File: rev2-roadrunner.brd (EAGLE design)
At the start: 49.5 x 34.3 mm, 22 parts, among them J1 USB_MINI-B_SMT, Y1 16MHz

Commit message: Finalized Board and Schematic design
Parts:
- added C4: 0.1uF, SparkFun-Capacitors:1206
- added C5: 1.0uF, SparkFun-Capacitors:1206
- added D4: WS2812B, SparkFun-LED:WS2812B
- added F1: 6V/0.5A, SparkFun-Fuses:1206
- D7: value GREEN -> Yellow
- J2: device SparkFun-Connectors:1X03 -> SparkFun-Connectors:1X07
- J3: device SparkFun-Connectors:1X14 -> SparkFun-Connectors:1X10
- J4: device SparkFun-Connectors:1X04 -> SparkFun-Connectors:1X06
- moved J4 43.9 mm to (3.30, 2.16), turned to 0 degrees
- moved J3 29.5 mm to (47.0, 2.54), turned to 90 degrees
- moved R7 25.0 mm to (36.9, 9.43), turned to 180 degrees
- moved D1 23.4 mm to (27.1, 30.7)
- moved R3 21.0 mm to (24.4, 30.8), turned to 270 degrees
- moved D7 19.2 mm to (36.9, 12.7)
- moved S1 18.3 mm to (37.5, 4.03), turned to 0 degrees
- moved C1 13.7 mm to (14.0, 25.9), turned to 180 degrees
- moved J2 11.9 mm to (47.0, 31.8), turned to 180 degrees
- moved D3 10.7 mm to (5.59, 32.0), turned to 180 degrees
- moved C2 5.18 mm to (12.7, 30.5), turned to 90 degrees
- moved R8 4.05 mm to (13.9, 9.27), turned to 0 degrees
- moved ICSP 2.54 mm to (6.00, 9.04)
- moved D2 2.51 mm to (14.2, 12.3), turned to 180 degrees
- moved R4 2.36 mm to (13.9, 22.1)
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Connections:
- net USBD1_N renamed USB_D1_N
- net USBD1_P renamed USB_D1_P
- net USBD_N renamed USB_D_N
- net USBD_P renamed USB_D_P
- new net N$4: D3.A, F1.2
- new net USB_VCC: F1.1, J1.VBUS
- net 5V: now also C2.1, C4.1, C5.1, D2.A, D4.1, D7.A, J2.7, R3.2; no longer C2.2, J1.VBUS, J3.14, R7.2
- net AREF: now also J2.5; no longer J3.12
- net GND: now also C2.2, C4.2, C5.2, D4.3, J2.6; no longer C2.1, D2.C, D3.A, D7.C, J3.13
- net N$2: now also D7.C, R7.1; no longer D2.A, R2.1
- net N$3: now also D2.C, R2.2; no longer D7.A, R7.1
- net PB4: now also J3.4; no longer J3.1
- net PB5: now also J3.5; no longer J3.2
- net PB6: now also J3.6; no longer J3.3
- net PB7: now also J4.6
- net PC6: now also J3.7; no longer J3.4
- net PC7: now also J3.8; no longer J3.5
- net PD4: now also J3.1; no longer J2.1
- net PD6: now also J3.2; no longer J2.2
- net PD7: now also J3.3; no longer J2.3
- net PE6: now also J4.5
- net PF0: now also J2.4; no longer J3.11
- net PF1: now also J2.3; no longer J3.10
- net PF4: now also J2.2; no longer J3.9
- net PF5: now also J2.1; no longer J3.8
- net PF6: now also J3.10; no longer J3.7
- net PF7: now also D4.4, J3.9; no longer J3.6
- net RX_LED: now also R2.1; no longer R2.2
- net TX_LED: now also R7.2; no longer R3.2
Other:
- board text added: "IEEE Carleton PCB Workshop Fall 2017"
- board text added: "PB7"
- board text added: "PE6"
- board text added: "RoadRunner"

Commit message: Before Autorouter
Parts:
- moved R1 0.25 mm to (13.9, 18.3)
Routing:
- net 5V: track 0.00 -> 24.9 mm
- net XTAL_N: track 0.00 -> 9.36 mm
- net XTAL_P: track 0.00 -> 9.27 mm
- net USB_VCC: track 0.00 -> 8.90 mm
- net USB_D1_N: track 0.00 -> 5.25 mm
- net USB_D1_P: track 0.00 -> 5.22 mm
- net USB_D_N: track 0.00 -> 4.67 mm
- net USB_D_P: track 0.00 -> 4.64 mm
- net N$4: track 0.00 -> 3.66 mm
- net N$1: track 0.00 -> 2.73 mm
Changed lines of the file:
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@@
 <?xml version="1.0" encoding="utf-8"?>
 <!DOCTYPE eagle SYSTEM "eagle.dtd">
-<eagle version="8.3.0">
+<eagle version="8.2.2">
 <drawing>
 <settings>
 <setting alwaysvectorfont="no"/>
-<setting keepoldvectorfont="yes"/>
 <setting verticaltext="up"/>
 </settings>
-<grid distance="0.05" unitdist="inch" unit="mil" style="lines" multiple="1" display="yes" altdistance="0.005" altunitdist="inch" altunit="mil"/>
+<grid distance="50" unitdist="mil" unit="mil" style="lines" multiple="1" display="yes" altdistance="0.005" altunitdist="inch" altunit="mil"/>
 <layers>
 <layer number="1" name="Top" color="4" fill="1" visible="yes" active="yes"/>
@@
 <attribute name="PROD_ID" value="CAP-10057" x="12.667284375" y="30.4521625" size="1.778" layer="27" rot="R90" display="off"/>
 </element>
-<element name="R1" library="SparkFun-Resistors" package="1206" value=" 22" x="13.9421625" y="18.574715625" smashed="yes">
-<attribute name="NAME" x="14.0691625" y="17.177715625" size="0.6096" layer="25" font="vector" ratio="20" align="bottom-center"/>
-<attribute name="PROD_ID" value=" " x="13.9421625" y="18.574715625" size="1.778" layer="27" display="off"/>
+<element name="R1" library="SparkFun-Resistors" package="1206" value=" 22" x="13.9421625" y="18.320715625" smashed="yes">
+<attribute name="NAME" x="14.0691625" y="16.923715625" size="0.6096" layer="25" font="vector" ratio="20" align="bottom-center"/>
+<attribute name="PROD_ID" value=" " x="13.9421625" y="18.320715625" size="1.778" layer="27" display="off"/>
 </element>
 <element name="R4" library="SparkFun-Resistors" package="1206" value=" 22" x="13.9421625" y="22.130715625" smashed="yes">
@@
 <contactref element="Y1" pad="1"/>
 <contactref element="C3" pad="2"/>
-<wire x1="27.0201625" y1="9.303715625" x2="25.7531625" y2="12.393715625" width="0" layer="19" extent="1-1"/>
-<wire x1="27.7851625" y1="3.969715625" x2="27.0201625" y2="9.303715625" width="0" layer="19" extent="1-1"/>
+<wire x1="25.7531625" y1="12.393715625" x2="25.7531625" y2="10.570715625" width="0.254" layer="1"/>
+<wire x1="25.7531625" y1="10.570715625" x2="27.0201625" y2="9.303715625" width="0.254" layer="1"/>
+<wire x1="27.0201625" y1="9.303715625" x2="27.0201625" y2="4.734715625" width="0.254" layer="1"/>
+<wire x1="27.0201625" y1="4.734715625" x2="27.7851625" y2="3.969715625" width="0.254" layer="1"/>
 </signal>
 <signal name="XTAL_N">
@@
 <contactref element="Y1" pad="2"/>
 <contactref element="C6" pad="2"/>
-<wire x1="23.7241625" y1="9.303715625" x2="24.9531625" y2="12.393715625" width="0" layer="19" extent="1-1"/>
-<wire x1="22.7051625" y1="3.969715625" x2="23.7241625" y2="9.303715625" width="0" layer="19" extent="1-1"/>
+<wire x1="24.9531625" y1="12.393715625" x2="24.9531625" y2="10.532715625" width="0.254" layer="1"/>
+<wire x1="24.9531625" y1="10.532715625" x2="23.7241625" y2="9.303715625" width="0.254" layer="1"/>
+<wire x1="23.7241625" y1="9.303715625" x2="23.7241625" y2="4.988715625" width="0.254" layer="1"/>
+<wire x1="23.7241625" y1="4.988715625" x2="22.7051625" y2="3.969715625" width="0.254" layer="1"/>
 </signal>
 <signal name="MISO">
@@
 <contactref element="J2" pad="7"/>
 <contactref element="D4" pad="1"/>
+<wire x1="6.738" y1="32.004" x2="7.366" y2="32.004" width="0.508" layer="1"/>
+<wire x1="7.366" y1="32.004" x2="10.16" y2="29.21" width="0.508" layer="1"/>
+<wire x1="10.16" y1="29.21" x2="12.509446875" y2="29.21" width="0.508" layer="1"/>
+<wire x1="12.509446875" y1="29.21" x2="12.667284375" y2="29.0521625" width="0.508" layer="1"/>
+<wire x1="12.667284375" y1="29.0521625" x2="15.8471625" y2="29.0521625" width="0.508" layer="1"/>
+<wire x1="15.8471625" y1="29.0521625" x2="15.875" y2="29.08" width="0.508" layer="1"/>
+<wire x1="15.875" y1="29.08" x2="19.685" y2="29.08" width="0.508" layer="1"/>
+<wire x1="19.685" y1="29.08" x2="19.685" y2="26.061878125" width="0.508" layer="1"/>
+<wire x1="19.685" y1="26.061878125" x2="21.7531625" y2="23.993715625" width="0.508" layer="1"/>
+<wire x1="19.685" y1="29.08" x2="24.029871875" y2="29.08" width="0.508" layer="1"/>
+<wire x1="24.029871875" y1="29.08" x2="24.351284375" y2="29.4014125" width="0.508" layer="1"/>
 <wire x1="24.351284375" y1="29.4014125" x2="31.75" y2="31.75" width="0" layer="19" extent="1-1"/>
-<wire x1="19.685" y1="29.08" x2="24.351284375" y2="29.4014125" width="0" layer="19" extent="1-1"/>
-<wire x1="15.875" y1="29.08" x2="19.685" y2="29.08" width="0" layer="19" extent="1-1"/>
-<wire x1="12.667284375" y1="29.0521625" x2="15.875" y2="29.08" width="0" layer="19" extent="1-1"/>
-<wire x1="21.7531625" y1="23.993715625" x2="19.685" y2="29.08" width="0" layer="19" extent="1-1"/>
 <wire x1="19.9531625" y1="21.393715625" x2="21.7531625" y2="23.993715625" width="0" layer="19" extent="1-1"/>
 <wire x1="19.9531625" y1="17.393715625" x2="19.9531625" y2="21.393715625" width="0" layer="19" extent="1-1"/>
 <wire x1="23.3531625" y1="12.393715625" x2="19.9531625" y2="17.393715625" width="0" layer="19" extent="1-1"/>
-<wire x1="6.738" y1="32.004" x2="12.667284375" y2="29.0521625" width="0" layer="19" extent="1-1"/>
 <wire x1="15.691284375" y1="12.2911625" x2="19.9531625" y2="17.393715625" width="0" layer="19" extent="1-1"/>
 <wire x1="15.3421625" y1="9.271965625" x2="15.691284375" y2="12.2911625" width="0" layer="19" extent="1-1"/>
 <wire x1="29.7531625" y1="23.993715625" x2="24.351284375" y2="29.4014125" width="0" layer="19" extent="1-1"/>
-<wire x1="31.5531625" y1="14.993715625" x2="23.3531625" y2="12.393715625" width="0" layer="19" extent="1-1"/>
+<wire x1="35.484" y1="20.41" x2="29.7531625" y2="23.993715625" width="0" layer="19" extent="1-1"/>
+<wire x1="31.5531625" y1="14.993715625" x2="35.484" y2="20.41" width="0" layer="19" extent="1-1"/>
 <wire x1="35.424284375" y1="12.6721625" x2="31.5531625" y2="14.993715625" width="0" layer="19" extent="1-1"/>
-<wire x1="35.484" y1="20.41" x2="29.7531625" y2="23.993715625" width="0" layer="19" extent="1-1"/>
 <wire x1="4.731715625" y1="6.5048375" x2="15.3421625" y2="9.271965625" width="0" layer="19" extent="1-1"/>
 </signal>
@@
 <contactref element="R3" pad="1"/>
 <contactref element="D1" pad="A"/>
-<wire x1="24.351284375" y1="32.2014125" x2="27.0788375" y2="32.201284375" width="0" layer="19" extent="1-1"/>
+<wire x1="24.351284375" y1="32.2014125" x2="27.078709375" y2="32.2014125" width="0.508" layer="1"/>
+<wire x1="27.078709375" y1="32.2014125" x2="27.0788375" y2="32.201284375" width="0.508" layer="1"/>
 </signal>
 <signal name="RX_LED">
@@
 <contactref element="J1" pad="D-"/>
 <contactref element="R4" pad="1"/>
-<wire x1="8.514315625" y1="20.589015625" x2="12.5421625" y2="22.130715625" width="0" layer="19" extent="1-1"/>
+<wire x1="8.514315625" y1="20.589015625" x2="11.0004625" y2="20.589015625" width="0.508" layer="1"/>
+<wire x1="11.0004625" y1="20.589015625" x2="12.5421625" y2="22.130715625" width="0.508" layer="1"/>
 </signal>
 <signal name="USB_VCC" class="3">
 <contactref element="J1" pad="VBUS"/>
 <contactref element="F1" pad="1"/>
-<wire x1="8.514315625" y1="21.389015625" x2="7.496" y2="28.448" width="0" layer="19" extent="1-1"/>
+<wire x1="7.496" y1="28.448" x2="7.496" y2="28.2039125" width="0.508" layer="1"/>
+<wire x1="7.496" y1="28.2039125" x2="10.221515625" y2="25.478396875" width="0.508" layer="1"/>
+<wire x1="10.221515625" y1="23.096215625" x2="8.514315625" y2="21.389015625" width="0.508" layer="1"/>
+<wire x1="10.221515625" y1="25.478396875" x2="10.221515625" y2="23.096215625" width="0.508" layer="1"/>
 </signal>
 <signal name="USB_D_P">
 <contactref element="J1" pad="D+"/>
 <contactref element="R1" pad="1"/>
-<wire x1="8.514315625" y1="19.789015625" x2="12.5421625" y2="18.574715625" width="0" layer="19" extent="1-1"/>
+<wire x1="8.514315625" y1="19.789015625" x2="11.0738625" y2="19.789015625" width="0.508" layer="1"/>
+<wire x1="11.0738625" y1="19.789015625" x2="12.5421625" y2="18.320715625" width="0.508" layer="1"/>
 </signal>
 <signal name="USB_D1_P">
 <contactref element="R1" pad="2"/>
 <contactref element="U$1" pad="4"/>
-<wire x1="15.3421625" y1="18.574715625" x2="19.9531625" y2="19.793715625" width="0" layer="19" extent="1-1"/>
+<wire x1="19.9531625" y1="19.793715625" x2="16.8151625" y2="19.793715625" width="0.508" layer="1"/>
+<wire x1="16.8151625" y1="19.793715625" x2="15.3421625" y2="18.320715625" width="0.508" layer="1"/>
 </signal>
 <signal name="USB_D1_N">
 <contactref element="R4" pad="2"/>
 <contactref element="U$1" pad="3"/>
-<wire x1="15.3421625" y1="22.130715625" x2="19.9531625" y2="20.593715625" width="0" layer="19" extent="1-1"/>
+<wire x1="19.9531625" y1="20.593715625" x2="16.8791625" y2="20.593715625" width="0.508" layer="1"/>
+<wire x1="16.8791625" y1="20.593715625" x2="15.3421625" y2="22.130715625" width="0.508" layer="1"/>
 </signal>
 <signal name="N$4">
 <contactref element="F1" pad="2"/>
 <contactref element="D3" pad="A"/>
-<wire x1="4.696" y1="28.448" x2="4.438" y2="32.004" width="0" layer="19" extent="1-1"/>
+<wire x1="4.438" y1="32.004" x2="4.438" y2="28.706" width="0.508" layer="1"/>
+<wire x1="4.438" y1="28.706" x2="4.696" y2="28.448" width="0.508" layer="1"/>
 </signal>
 <signal name="N$2">
@@
 </note>
 <note version="8.2" severity="warning">
-Since Version 8.2, EAGLE supports online libraries. The ids
+Since Version 8.2, Eagle supports online libraries. The ids
 of those online libraries will not be understood (or retained)
 with this version.

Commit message: Fixed Routes after Autorouter
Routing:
- net 5V: track 24.9 -> 102.3 mm
- net PD1: track 0.00 -> 48.7 mm, vias 0 -> 1
- net RST: track 0.00 -> 45.0 mm, vias 0 -> 1
- net PE6: track 0.00 -> 40.6 mm, vias 0 -> 1
- net PD0: track 0.00 -> 36.3 mm, vias 0 -> 2
- net PD7: track 0.00 -> 34.8 mm
- net TX: track 0.00 -> 33.9 mm
- net PB4: track 0.00 -> 31.5 mm, vias 0 -> 1
- net PF4: track 0.00 -> 29.0 mm, vias 0 -> 1
- net PD6: track 0.00 -> 28.8 mm, vias 0 -> 1
- net RX: track 0.00 -> 28.3 mm, vias 0 -> 1
- net PD4: track 0.00 -> 26.0 mm, vias 0 -> 1
- net PF5: track 0.00 -> 24.8 mm, vias 0 -> 2
- net PF0: track 0.00 -> 24.2 mm, vias 0 -> 1
- net PF1: track 0.00 -> 23.7 mm, vias 0 -> 1
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- added copper zone on layer 1, net GND
- added copper zone on layer 16, net GND
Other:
- board text added: "VCC"

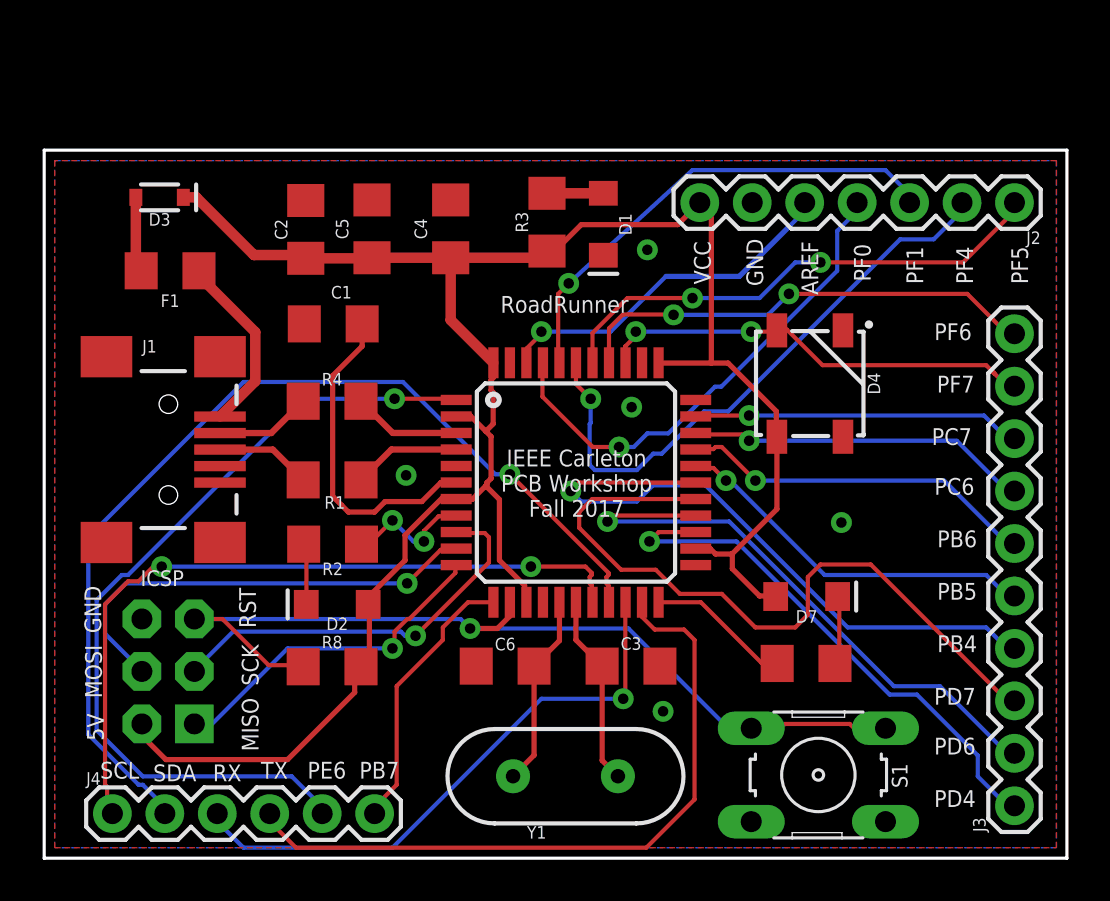
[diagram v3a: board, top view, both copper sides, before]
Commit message: Added attributes for crystal
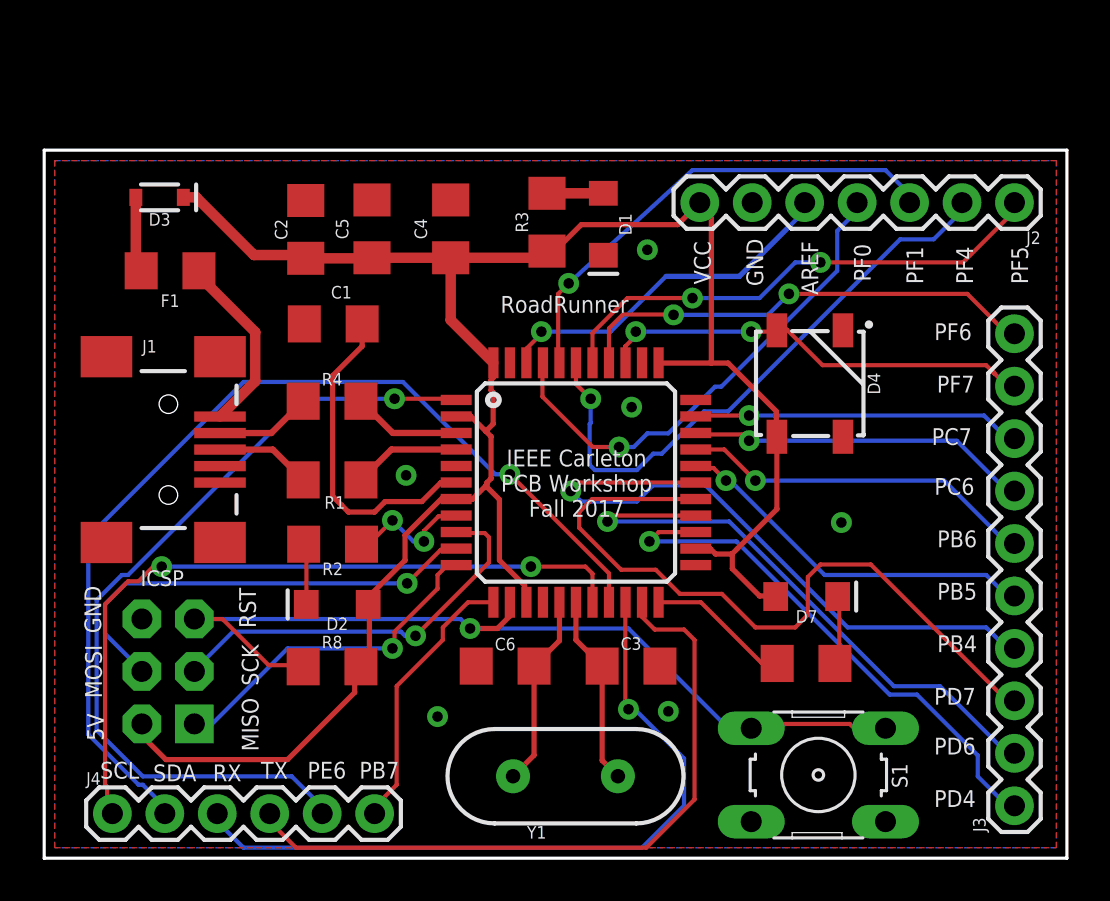
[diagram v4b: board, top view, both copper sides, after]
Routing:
- net RX: track 28.3 -> 35.6 mm

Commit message: Re-routed by hand + Moved C1 down
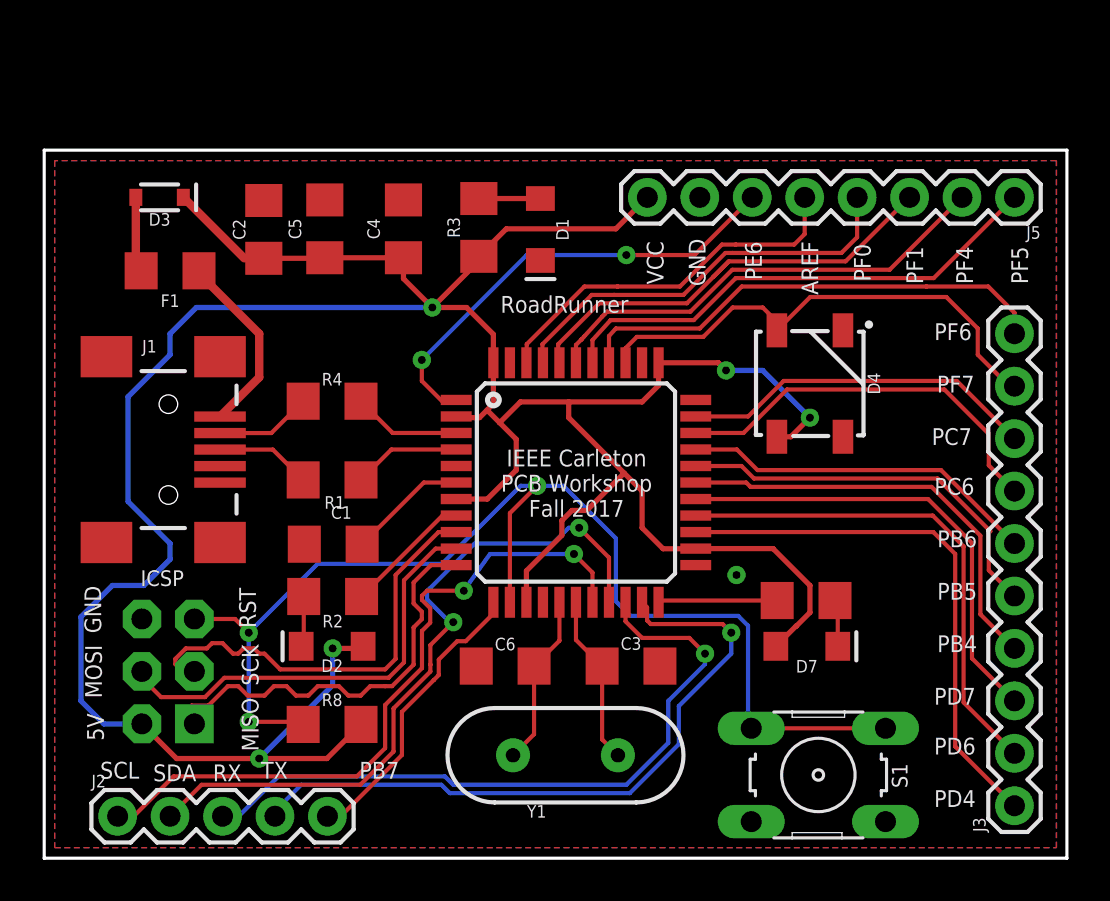
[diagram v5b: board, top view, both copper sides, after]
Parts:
- removed J4: (no value), SparkFun-Connectors:1X06
- added J5: (no value), SparkFun-Connectors:1X08
- J2: device SparkFun-Connectors:1X07 -> SparkFun-Connectors:1X05
- moved J2 52.6 mm to (3.56, 2.03), turned to 0 degrees
- moved C1 10.7 mm to (14.0, 15.2)
- moved R3 3.31 mm to (21.0, 30.5)
- moved D1 3.06 mm to (24.0, 30.4)
- moved R7 3.05 mm to (36.9, 12.5)
- moved R8 2.79 mm to (13.9, 6.48)
- moved R2 2.53 mm to (14.0, 12.7)
- moved D7 2.41 mm to (36.9, 10.3)
- moved C5 2.29 mm to (13.6, 30.5)
- moved C4 2.29 mm to (17.4, 30.5)
- moved D2 2.04 mm to (13.9, 10.3)
- moved C2 2.03 mm to (10.6, 30.5)
- moved Y1 1.02 mm to (25.2, 4.99)
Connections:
- net 5V: now also J5.8; no longer J2.7
- net AREF: now also J5.5; no longer J2.5
- net GND: now also J5.7; no longer J2.6
- net PB7: now also J2.5; no longer J4.6
- net PD0: now also J2.1; no longer J4.1
- net PD1: now also J2.2; no longer J4.2
- net PE6: now also J5.6; no longer J4.5
- net PF0: now also J5.4; no longer J2.4
- net PF1: now also J5.3; no longer J2.3
- net PF4: now also J5.2; no longer J2.2
- net PF5: now also J5.1; no longer J2.1
- net RX: now also J2.3; no longer J4.3
- net TX: now also J2.4; no longer J4.4
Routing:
- net 5V: track 102.3 -> 151.9 mm, vias 0 -> 5
- net PE6: track 40.6 -> 22.4 mm, vias 1 -> 2
- net RST: track 45.0 -> 59.3 mm, vias 1 -> 3
- net PD1: track 48.6 -> 34.6 mm, vias 1 -> 2
- net PD7: track 34.8 -> 22.8 mm
- net PB4: track 31.5 -> 21.0 mm, vias 1 -> 0
- net UCAP: track 15.8 -> 5.79 mm
- net PF4: track 29.0 -> 22.7 mm, vias 1 -> 0
- net MISO: track 16.7 -> 21.3 mm, vias 1 -> 0
- net PD6: track 28.8 -> 24.6 mm, vias 1 -> 0
- net PF0: track 24.2 -> 20.2 mm, vias 1 -> 0
- net PF7: track 21.5 -> 24.3 mm, vias 2 -> 0
- net PC6: track 16.6 -> 19.2 mm, vias 1 -> 0
- net PD0: track 36.2 -> 33.9 mm
- net RX: track 35.6 -> 33.9 mm
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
